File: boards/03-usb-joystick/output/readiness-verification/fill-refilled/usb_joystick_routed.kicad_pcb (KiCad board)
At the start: 4 copper layers, 80 x 60 mm, 38 parts, among them J1 USB4085-GF-A, J2 Joystick 5V X Y SW, J3 AVR ISP, SW1 TL3342F160QG, SW2 TL3342F160QG, SW3 TL3342F160QG, SW4 TL3342F160QG, SW5 TL3342F160QG, U1 ATMEGA32U4-AU, U2 USBLC6-2SC6, Y1 8MHz

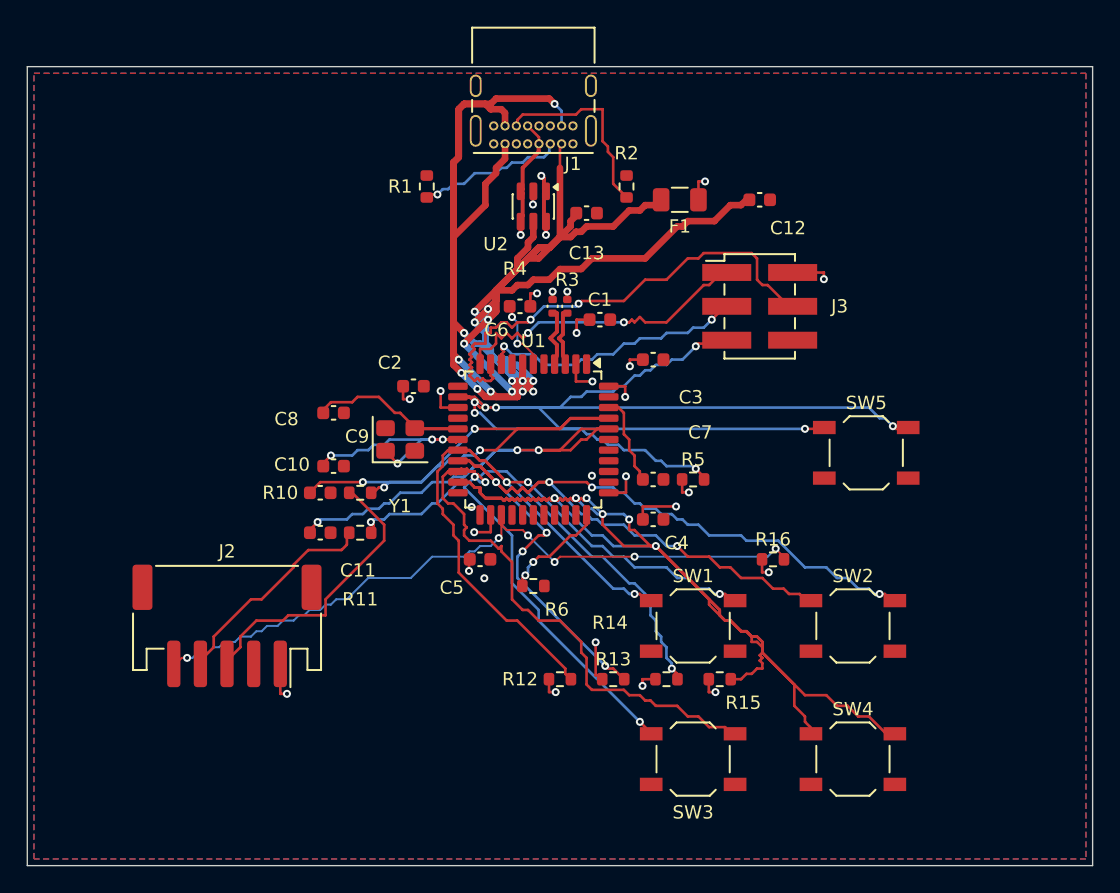
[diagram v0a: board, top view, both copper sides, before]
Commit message: fix(board03): re-derive committed copper from the arm C route and retire the USB_D via-count exception
USB_D+/USB_D- now carry 3/3 vias, so the #7108 via-count exception module,
its tests and the four callers' filters are deleted. Plan re-derived from the
arm C lattice route (jlcpcb, seed 42, C7498 keepout input) with reviewed
silk text and USB_MCU_D hand copper re-applied; tests pinned to the old
copper updated.

Co-Authored-By: Claude Sonnet 5.5 <noreply@anthropic.com>
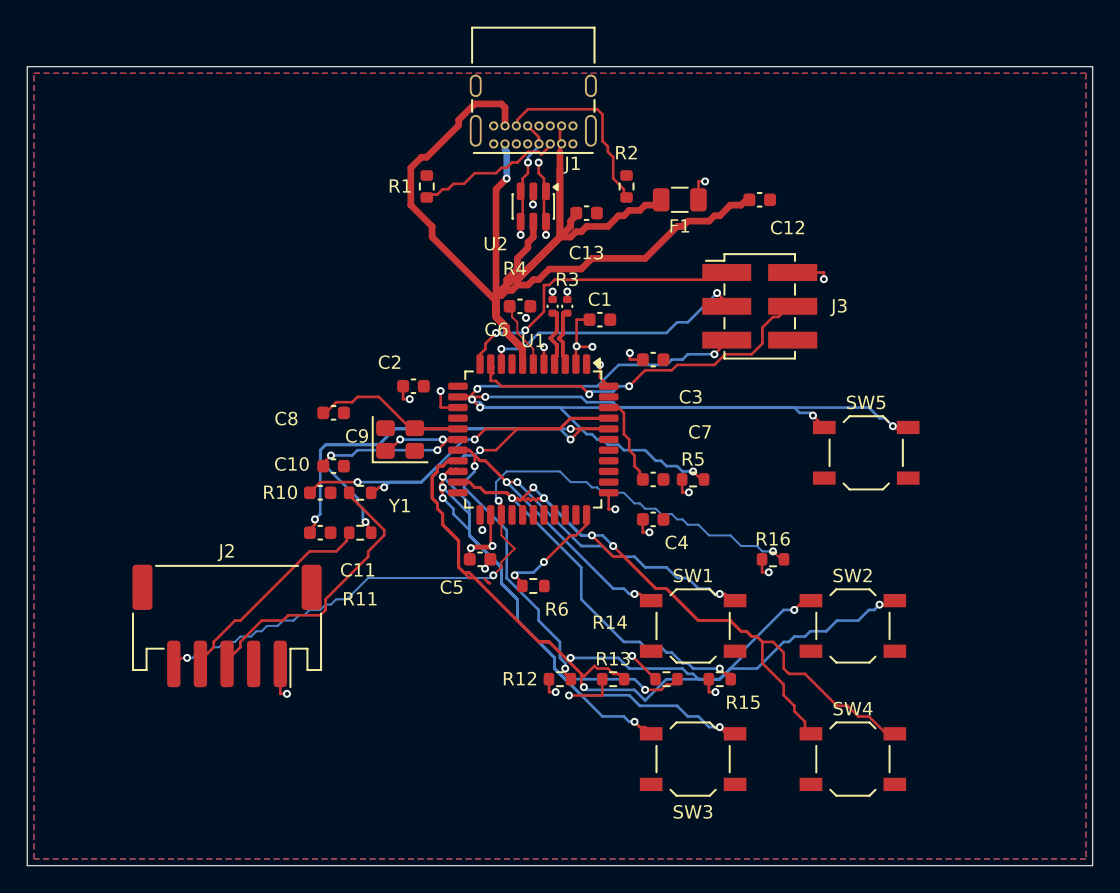
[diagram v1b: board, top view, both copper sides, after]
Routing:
- net VBUS: track 217.9 -> 164.3 mm, vias 17 -> 1
- net BTN2: track 95.4 -> 121.1 mm, vias 8 -> 4
- net JOY_Y: track 47.5 -> 59.7 mm
- net BTN4: track 119.4 -> 108.0 mm
- net ISP_MOSI: track 37.3 -> 28.2 mm
- net JOY_BTN: track 54.4 -> 59.8 mm, vias 6 -> 4
- net VCC: track 39.1 -> 42.3 mm
- net RESET: track 107.7 -> 106.4 mm
- net BTN3: track 93.2 -> 94.4 mm, vias 4 -> 6
- net BTN1: track 67.8 -> 66.7 mm, vias 4 -> 6
- net ISP_MISO: track 24.4 -> 23.3 mm
- net XTAL1: track 18.1 -> 17.3 mm
- net HWB: track 8.16 -> 8.90 mm
- net JOY_X_RAW: track 21.8 -> 21.2 mm
- net JOY_Y_RAW: track 16.4 -> 15.9 mm
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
